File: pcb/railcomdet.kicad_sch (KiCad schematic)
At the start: 3 parts

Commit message: Finished MTB part.
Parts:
- gave numbers to parts that had none: 3
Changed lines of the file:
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@@
   (symbol (lib_id "Connector:Screw_Terminal_01x04") (at 269.875 23.495 0) (unit 1)
     (in_bom yes) (on_board yes) (dnp no) (fields_autoplaced)
-    (property "Reference" "J?" (at 271.907 23.9303 0)
+    (property "Reference" "J1" (at 271.907 23.9303 0)
       (effects (font (size 1.27 1.27)) (justify left))
     )
@@
       (project "railcomdet"
         (path "/3e59d29f-2657-4552-9290-3c54fadfdf63"
-          (reference "J?") (unit 1)
+          (reference "J1") (unit 1)
         )
       )
@@
   (symbol (lib_id "Isolator:6N137") (at 144.145 109.22 0) (unit 1)
     (in_bom yes) (on_board yes) (dnp no) (fields_autoplaced)
-    (property "Reference" "U?" (at 144.145 97.9002 0)
+    (property "Reference" "U2" (at 144.145 97.9002 0)
       (effects (font (size 1.27 1.27)))
     )
@@
       (project "railcomdet"
         (path "/3e59d29f-2657-4552-9290-3c54fadfdf63"
-          (reference "U?") (unit 1)
+          (reference "U2") (unit 1)
         )
       )
@@
   (symbol (lib_id "Isolator:6N137") (at 144.145 60.96 0) (unit 1)
     (in_bom yes) (on_board yes) (dnp no) (fields_autoplaced)
-    (property "Reference" "U?" (at 144.145 49.6402 0)
+    (property "Reference" "U1" (at 144.145 49.6402 0)
       (effects (font (size 1.27 1.27)))
     )
@@
       (project "railcomdet"
         (path "/3e59d29f-2657-4552-9290-3c54fadfdf63"
-          (reference "U?") (unit 1)
+          (reference "U1") (unit 1)
         )
       )

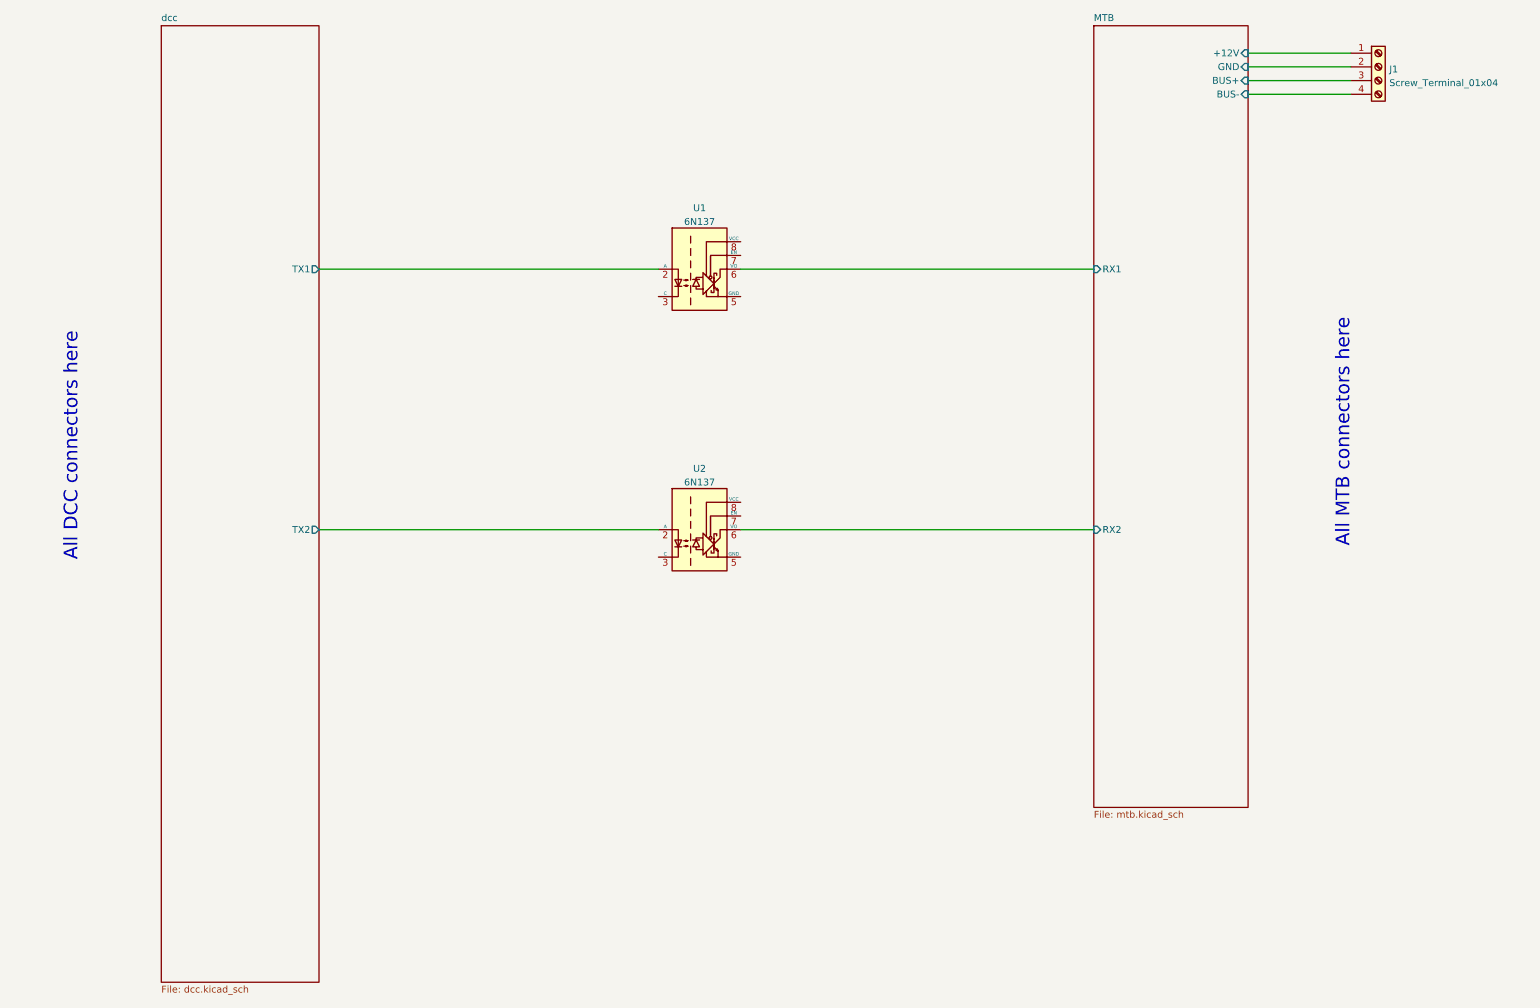
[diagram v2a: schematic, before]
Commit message: Connect DCC and MTB parts.
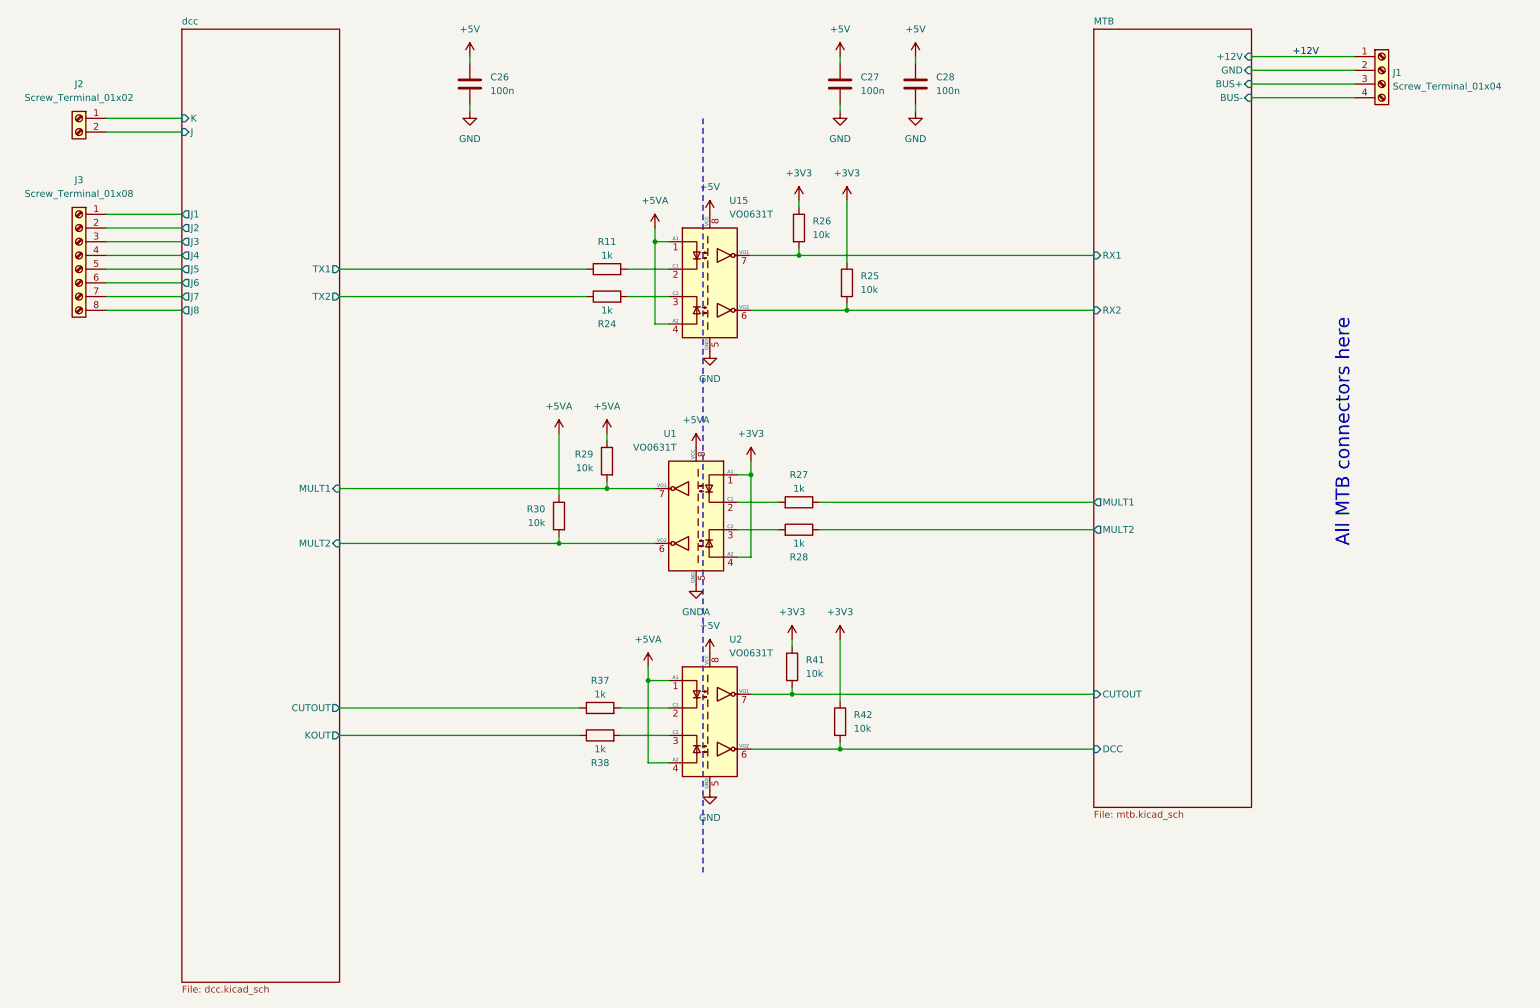
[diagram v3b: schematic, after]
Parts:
- removed U1, U2: 6N137, Package_DIP:DIP-8_W7.62mm, symbol Isolator:6N137
- added C26, C27, C28: 100n, symbol Device:C
- added J2: Screw_Terminal_01x02, symbol Connector:Screw_Terminal_01x02
- added J3: Screw_Terminal_01x08, symbol Connector:Screw_Terminal_01x08
- added R11, R24, R27, R28, R37, R38: 1k, symbol Device:R
- added R25, R26, R29, R30, R41, R42: 10k, symbol Device:R
- added U1, U15, U2: VO0631T, Package_SO:SOIC-8_3.9x4.9mm_P1.27mm, symbol Isolator:VO0631T
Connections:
- net MTB/RX1: now also R26.2, U15.7 (VO1)
- net MTB/RX2: now also R25.2, U15.6 (VO2)
- net dcc/TX1: now also R11.1
- net dcc/TX2: now also R24.1
- net MTB/+12V renamed +12V
- new net: R27.2, U1.2 (C1)
- new net: R11.2, U15.2 (C1)
- new net: R24.2, U15.3 (C2)
- new net: R28.2, U1.3 (C2)
- new net: R37.2, U2.2 (C1)
- new net: R38.2, U2.3 (C2)
- new net +3V3: R25.1, R26.1, R41.1, R42.1, U1.1 (A1), U1.4 (A2)
- new net +5V: C26.1, C27.1, C28.1, U15.8 (VCC), U2.8 (VCC)
- new net +5VA: R29.1, R30.1, U1.8 (VCC), U15.1 (A1), U15.4 (A2), U2.1 (A1), U2.4 (A2)
- new net GND: C26.2, C27.2, C28.2, U15.5 (GND), U2.5 (GND)
- new net GNDA: U1.5 (GND)
- new net MTB/CUTOUT: R41.2, U2.7 (VO1)
- new net MTB/DCC: R42.2, U2.6 (VO2)
- new net MTB/MULT1: R27.1
- new net MTB/MULT2: R28.1
- new net dcc/CUTOUT: R37.1
- new net dcc/J: J2.2 (Pin_2)
- new net dcc/J1: J3.1 (Pin_1)
- new net dcc/J2: J3.2 (Pin_2)
- new net dcc/J3: J3.3 (Pin_3)
- new net dcc/J4: J3.4 (Pin_4)
- new net dcc/J5: J3.5 (Pin_5)
- new net dcc/J6: J3.6 (Pin_6)
- new net dcc/J7: J3.7 (Pin_7)
- new net dcc/J8: J3.8 (Pin_8)
- new net dcc/K: J2.1 (Pin_1)
- new net dcc/KOUT: R38.1
- new net dcc/MULT1: R29.2, U1.7 (VO1)
- new net dcc/MULT2: R30.2, U1.6 (VO2)
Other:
- sheet MTB ports: added CUTOUT, DCC, MULT1, MULT2; removed none
- sheet dcc ports: added CUTOUT, J, J1, J2, J3, J4, J5, J6, J7, J8, K, KOUT, MULT1, MULT2; removed none
- note removed: "All DCC connectors here"
- moved on the sheet: J1

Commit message: Finished.
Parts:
- added C29: 1n, symbol Device:C
- added R44: 1k, symbol Device:R
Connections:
- net GND: now also C29.2
- net MTB/CUTOUT: now also C29.1, R44.2; no longer U2.7 (VO1)
- new net: R44.1, U2.7 (VO1)
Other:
- moved on the sheet: R41
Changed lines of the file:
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@@
   (junction (at 170.18 149.86) (diameter 0) (color 0 0 0 0)
   )
-  (junction (at 161.29 139.7) (diameter 0) (color 0 0 0 0)
-  )
   (junction (at 127 101.6) (diameter 0) (color 0 0 0 0)
   )
   (junction (at 171.45 68.58) (diameter 0) (color 0 0 0 0)
   )
+  (junction (at 200.66 139.7) (diameter 0) (color 0 0 0 0)
+  )
   (junction (at 153.67 99.06) (diameter 0) (color 0 0 0 0)
   )
@@
     (stroke (width 0) (type default))
   )
-  (wire (pts (xy 161.29 139.7) (xy 217.17 139.7))
-    (stroke (width 0) (type default))
-  )
-  (wire (pts (xy 161.29 129.54) (xy 161.29 130.81))
+  (wire (pts (xy 200.66 128.27) (xy 200.66 129.54))
     (stroke (width 0) (type default))
   )
@@
     (stroke (width 0) (type default))
   )
+  (wire (pts (xy 193.04 139.7) (xy 200.66 139.7))
+    (stroke (width 0) (type default))
+  )
   (wire (pts (xy 34.29 50.8) (xy 48.26 50.8))
     (stroke (width 0) (type default))
@@
     (stroke (width 0) (type default))
   )
+  (wire (pts (xy 200.66 140.97) (xy 200.66 139.7))
+    (stroke (width 0) (type default))
+  )
   (wire (pts (xy 135.89 71.12) (xy 138.43 71.12))
     (stroke (width 0) (type default))
@@
     (stroke (width 0) (type default))
   )
+  (wire (pts (xy 153.67 139.7) (xy 185.42 139.7))
+    (stroke (width 0) (type default))
+  )
   (wire (pts (xy 246.38 21.59) (xy 265.43 21.59))
     (stroke (width 0) (type default))
   )
+  (wire (pts (xy 200.66 139.7) (xy 217.17 139.7))
+    (stroke (width 0) (type default))
+  )
   (wire (pts (xy 34.29 35.56) (xy 48.26 35.56))
     (stroke (width 0) (type default))
@@
     (stroke (width 0) (type default))
   )
+  (wire (pts (xy 200.66 148.59) (xy 200.66 152.4))
+    (stroke (width 0) (type default))
+  )
   (wire (pts (xy 162.56 57.15) (xy 162.56 58.42))
     (stroke (width 0) (type default))
   )
-  (wire (pts (xy 161.29 138.43) (xy 161.29 139.7))
+  (wire (pts (xy 200.66 137.16) (xy 200.66 139.7))
     (stroke (width 0) (type default))
   )
@@
   )
   (wire (pts (xy 166.37 104.14) (xy 217.17 104.14))
-    (stroke (width 0) (type default))
-  )
-  (wire (pts (xy 153.67 139.7) (xy 161.29 139.7))
     (stroke (width 0) (type default))
   )
@@
     )
   )
+  (symbol (lib_id "power:GND") (at 200.66 152.4 0) (unit 1)
+    (in_bom yes) (on_board yes) (dnp no) (fields_autoplaced)
+    (property "Reference" "#PWR063" (at 200.66 158.75 0)
+      (effects (font (size 1.27 1.27)) hide)
+    )
+    (property "Value" "GND" (at 200.66 157.48 0)
+      (effects (font (size 1.27 1.27)))
+    )
+    (property "Footprint" "" (at 200.66 152.4 0)
+      (effects (font (size 1.27 1.27)) hide)
+    )
+    (property "Datasheet" "" (at 200.66 152.4 0)
+      (effects (font (size 1.27 1.27)) hide)
+    )
+    (pin "1")
+    (instances
+      (project "railcomdet"
+        (path "/3e59d29f-2657-4552-9290-3c54fadfdf63"
+          (reference "#PWR063") (unit 1)
+        )
+      )
+    )
+  )
   (symbol (lib_id "Device:C") (at 101.6 26.67 0) (unit 1)
     (in_bom yes) (on_board yes) (dnp no) (fields_autoplaced)
@@
     )
   )
-  (symbol (lib_id "Device:R") (at 161.29 134.62 0) (unit 1)
-    (in_bom yes) (on_board yes) (dnp no) (fields_autoplaced)
-    (property "Reference" "R41" (at 163.83 133.35 0)
-      (effects (font (size 1.27 1.27)) (justify left))
-    )
-    (property "Value" "10k" (at 163.83 135.89 0)
-      (effects (font (size 1.27 1.27)) (justify left))
-    )
-    (property "Footprint" "" (at 159.512 134.62 90)
-      (effects (font (size 1.27 1.27)) hide)
-    )
-    (property "Datasheet" "~" (at 161.29 134.62 0)
+  (symbol (lib_id "Device:R") (at 200.66 133.35 0) (unit 1)
+    (in_bom yes) (on_board yes) (dnp no) (fields_autoplaced)
+    (property "Reference" "R41" (at 203.2 132.08 0)
+      (effects (font (size 1.27 1.27)) (justify left))
+    )
+    (property "Value" "10k" (at 203.2 134.62 0)
+      (effects (font (size 1.27 1.27)) (justify left))
+    )
+    (property "Footprint" "" (at 198.882 133.35 90)
+      (effects (font (size 1.27 1.27)) hide)
+    )
+    (property "Datasheet" "~" (at 200.66 133.35 0)
       (effects (font (size 1.27 1.27)) hide)
     )
@@
     )
   )
+  (symbol (lib_id "Device:C") (at 200.66 144.78 0) (unit 1)
+    (in_bom yes) (on_board yes) (dnp no) (fields_autoplaced)
+    (property "Reference" "C29" (at 204.47 143.51 0)
+      (effects (font (size 1.27 1.27)) (justify left))
+    )
+    (property "Value" "1n" (at 204.47 146.05 0)
+      (effects (font (size 1.27 1.27)) (justify left))
+    )
+    (property "Footprint" "" (at 201.6252 148.59 0)
+      (effects (font (size 1.27 1.27)) hide)
+    )
+    (property "Datasheet" "~" (at 200.66 144.78 0)
+      (effects (font (size 1.27 1.27)) hide)
+    )
+    (pin "1")
+    (pin "2")
+    (instances
+      (project "railcomdet"
+        (path "/3e59d29f-2657-4552-9290-3c54fadfdf63"
+          (reference "C29") (unit 1)
+        )
+      )
+    )
+  )
   (symbol (lib_id "power:GND") (at 170.18 31.75 0) (unit 1)
     (in_bom yes) (on_board yes) (dnp no) (fields_autoplaced)
@@
     )
   )
-  (symbol (lib_id "power:+3V3") (at 161.29 129.54 0) (unit 1)
-    (in_bom yes) (on_board yes) (dnp no) (fields_autoplaced)
-    (property "Reference" "#PWR052" (at 161.29 133.35 0)
-      (effects (font (size 1.27 1.27)) hide)
-    )
-    (property "Value" "+3V3" (at 161.29 124.46 0)
-      (effects (font (size 1.27 1.27)))
-    )
-    (property "Footprint" "" (at 161.29 129.54 0)
-      (effects (font (size 1.27 1.27)) hide)
-    )
-    (property "Datasheet" "" (at 161.29 129.54 0)
+  (symbol (lib_id "power:+3V3") (at 200.66 128.27 0) (unit 1)
+    (in_bom yes) (on_board yes) (dnp no) (fields_autoplaced)
+    (property "Reference" "#PWR052" (at 200.66 132.08 0)
+      (effects (font (size 1.27 1.27)) hide)
+    )
+    (property "Value" "+3V3" (at 200.66 123.19 0)
+      (effects (font (size 1.27 1.27)))
+    )
+    (property "Footprint" "" (at 200.66 128.27 0)
+      (effects (font (size 1.27 1.27)) hide)
+    )
+    (property "Datasheet" "" (at 200.66 128.27 0)
       (effects (font (size 1.27 1.27)) hide)
     )
@@
         )
       )
+    )
+  )
+  (symbol (lib_id "Device:R") (at 189.23 139.7 90) (mirror x) (unit 1)
+    (in_bom yes) (on_board yes) (dnp no) (fields_autoplaced)
+    (property "Reference" "R44" (at 189.23 133.35 90)
+      (effects (font (size 1.27 1.27)))
+    )
+    (property "Value" "1k" (at 189.23 135.89 90)
+      (effects (font (size 1.27 1.27)))
+    )
+    (property "Footprint" "" (at 189.23 137.922 90)
+      (effects (font (size 1.27 1.27)) hide)
+    )
+    (property "Datasheet" "~" (at 189.23 139.7 0)
+      (effects (font (size 1.27 1.27)) hide)
+    )
+    (pin "1")
+    (pin "2")
+    (instances
+      (project "railcomdet"
+        (path "/3e59d29f-2657-4552-9290-3c54fadfdf63"
+          (reference "R44") (unit 1)
+        )
+      )

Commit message: Added description.
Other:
- company: (none) -> Laboratory of railway vehicles control
- title: (none) -> RailComDet - root
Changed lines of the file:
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@@
 (kicad_sch (version 20230121) (generator eeschema)
   (paper "A4")
+  (title_block
+    (title "RailComDet - root")
+    (date "2023-10-23")
+    (rev "1.0")
+    (company "Laboratory of railway vehicles control")
+    (comment 1 "Kateřina Hanáková")
+    (comment 2 "https://github.com/kmzbrnoI/railcomdet")
+    (comment 3 "https://creativecommons.org/licenses/by-sa/4.0/")
+    (comment 4 "Released under the Creative Commons Attribution-ShareAlike 4.0 License")
+  )
   (junction (at 118.11 111.76) (diameter 0) (color 0 0 0 0)
   )
